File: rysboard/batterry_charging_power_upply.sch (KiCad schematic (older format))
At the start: 8 parts

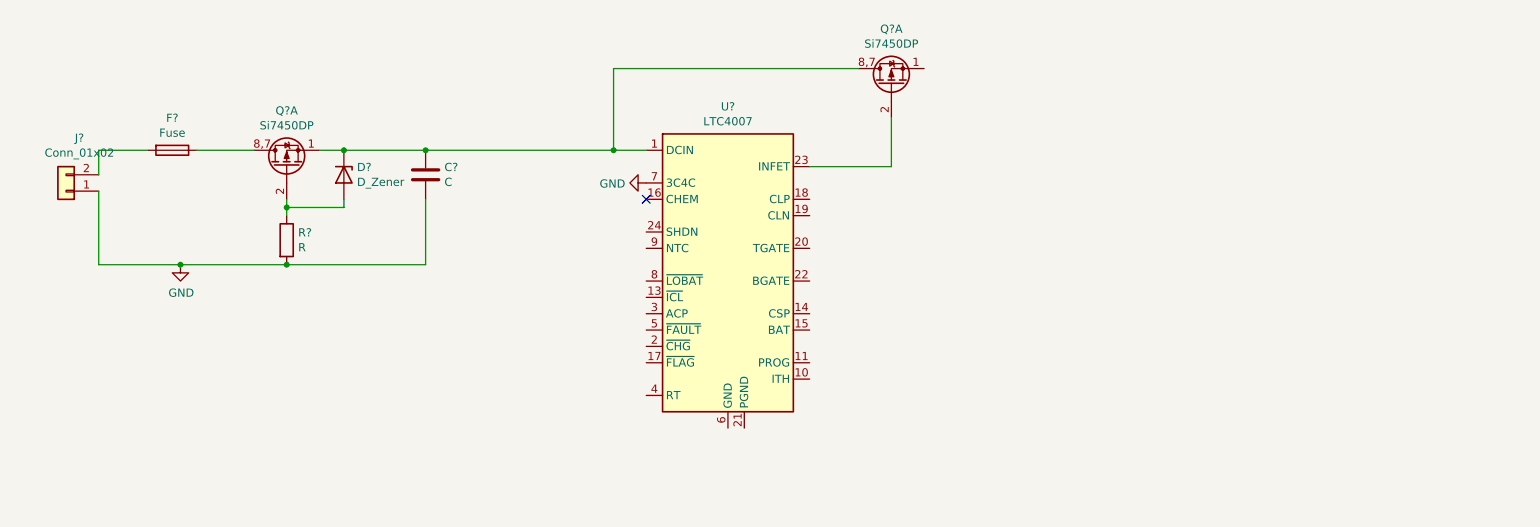
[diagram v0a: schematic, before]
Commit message: Added mcu, labeled its pins , major powwer supply overhaul started
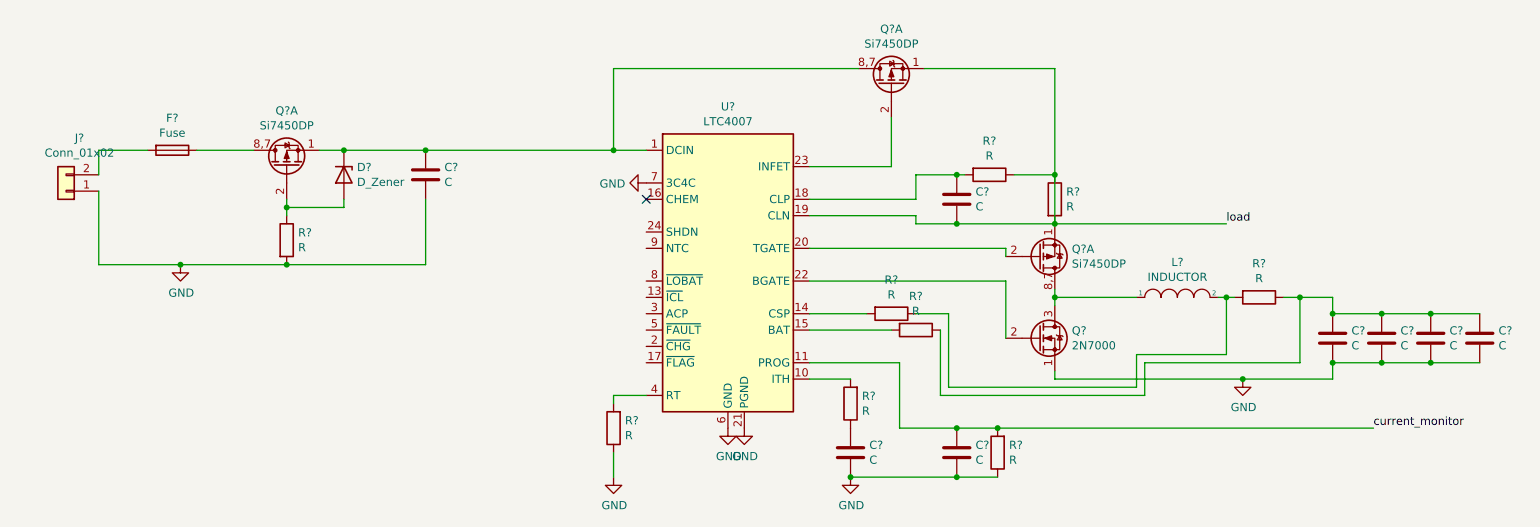
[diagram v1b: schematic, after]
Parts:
- added C? (x7): C, symbol Device:C
- added L?: INDUCTOR, symbol pspice:INDUCTOR
- added Q?: Si7450DP, Package_TO_SOT_SMD:SOT-23, symbol Transistor_FET:AO3401A
- added Q?: 2N7000, Package_TO_SOT_THT:TO-92_Inline, symbol Transistor_FET:2N7000
- added R? (x8): R, symbol Device:R
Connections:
- net GND: now also U?.21 (PGND), U?.6 (GND), C?.2, C?.2, C?.2, C?.2, C?.2, C?.2, Q?.1 (S), R?.1, R?.1
- net at U?.10 (ITH): now also R?.2
- net current_monitor: now reaches U?.11 (PROG)
- net current_monitor: now also C?.1, R?.2
- net at U?.14 (CSP): now also R?.2
- net at U?.15 (BAT): now also R?.2
- net at U?.18 (CLP): now also C?.1, R?.2
- net load: now reaches U?.19 (CLN)
- net load: now also Q?.1 (S1), C?.2, Q?.1 (S1), R?.1, R?.1, R?.2
- net at U?.20 (TGATE): now also Q?.2 (G1)
- net at U?.22 (BGATE): now also Q?.2 (G)
- net at U?.4 (RT): now also R?.2
- new net: L?.1, Q?.3 (D), Q?.8,7 (D1)
- new net: L?.2, R?.1, R?.2
- new net: C?.1, C?.1, C?.1, C?.1, R?.1, R?.1
- new net: C?.1, R?.1

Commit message: NST847BDP6T5G Added, more conections done
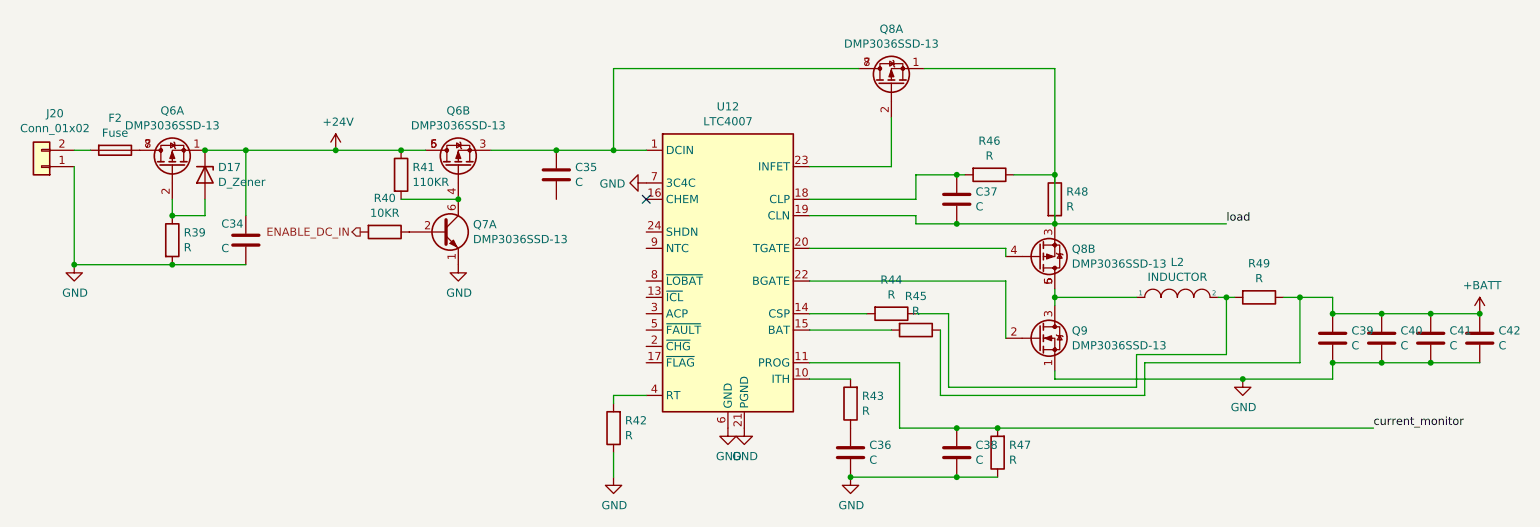
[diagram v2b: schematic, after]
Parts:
- removed Q? (x3): Si7450DP, Package_TO_SOT_SMD:SOT-23, symbol Transistor_FET:AO3401A
- added C34: C, symbol Device:C
- added Q6, Q8: DMP3036SSD-13, Package_SO:SO-8_5.3x6.2mm_P1.27mm, symbol rysboard:DMP3036SSD-13
- added Q7: DMP3036SSD-13, Package_SO:SO-8_5.3x6.2mm_P1.27mm, symbol rysboard:NST847BDP6T5G
- added R40: 10KR, symbol Device:R
- added R41: 110KR, symbol Device:R
- Q9: renamed from Q?; value 2N7000 -> DMP3036SSD-13; footprint Package_TO_SOT_THT:TO-92_Inline -> Package_SO:SO-8_5.3x6.2mm_P1.27mm
- gave numbers to parts that had none: 22
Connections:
- net GND: now also C34.2, Q7.1 (E1); no longer C35.2
- net load: now also Q8.1 (S1), Q8.3 (S2)
- net at C35.1, U12.1 (DCIN): now also Q6.3 (S2), Q8.7 (d), Q8.8 (d); no longer D17.1 (K)
- net at U12.20 (TGATE): now also Q8.4 (G2)
- net at U12.23 (INFET): now also Q8.2 (G1)
- net at D17.2 (A), R39.1: now also Q6.2 (G1)
- net at F2.1: now also Q6.7 (d), Q6.8 (d)
- net at L2.1, Q9.3 (D): now also Q8.5 (d), Q8.6 (d)
- net +BATT: now reaches C39.1, C40.1, C41.1, C42.1, R45.1, R49.1
- new net: Q6.4 (G2), Q7.6 (C1), R41.2
- new net: Q7.2 (B1), R40.1
- new net +24V: C34.1, D17.1 (K), Q6.1 (S1), Q6.5 (d), Q6.6 (d), R41.1
- new net ENABLE_DC_IN: R40.2
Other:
- moved on the sheet: C35, D17, F2, J20, R39

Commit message: created eval board for STM , added mcu, created controll section for TOFS and FAN. Added programming pinout, Remooved legacy spi interface, Removed addidtional i2c socket
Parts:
- removed Q7: DMP3036SSD-13, Package_SO:SO-8_5.3x6.2mm_P1.27mm, symbol rysboard:NST847BDP6T5G
- added Q?: NST847BDP6T5G, Package_TO_SOT_SMD:SOT-963, symbol rysboard:NST847BDP6T5G
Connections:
- net GND: now also C35.2, Q?.1 (E1)
- net at Q6.4 (G2), R41.2: now also Q?.6 (C1)
- net at R40.1: now also Q?.2 (B1)
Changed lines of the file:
@@
 $Descr A4 11693 8268
 encoding utf-8
-Sheet 4 6
+Sheet 4 7
 Title ""
 Date ""
@@
 	1650 1750 1550 1750
 $Comp
-L rysboard:NST847BDP6T5G Q7
-U 1 1 606ABC18
-P 3800 2250
-F 0 "Q7" H 3990 2296 50  0000 L CNN
-F 1 "DMP3036SSD-13" H 3990 2205 50  0000 L CNN
-F 2 "Package_SO:SO-8_5.3x6.2mm_P1.27mm" H 4000 2350 50  0001 C CNN
-F 3 "http://www.vishay.com/docs/70209/70209.pdf" H 3800 2250 50  0001 C CNN
-	1    3800 2250
-	1    0    0    -1
-$EndComp
-Connection ~ 3900 2050
-$Comp
 L power:GND #PWR041
 U 1 1 606AC403
@@
 	1    0    0    1
 $EndComp
+$Comp
+L rysboard:NST847BDP6T5G Q?
+U 1 1 606EA8D4
+P 3800 2250
+F 0 "Q?" H 3990 2296 50  0000 L CNN
+F 1 "NST847BDP6T5G" H 3990 2205 50  0000 L CNN
+F 2 "Package_TO_SOT_SMD:SOT-963" H 4000 2350 50  0001 C CNN
+F 3 "~" H 3800 2250 50  0001 C CNN
+	1    3800 2250
+	1    0    0    -1
+$EndComp
+Connection ~ 3900 2050
+$Comp
+L power:GND #PWR?
+U 1 1 606EB25B
+P 4500 2050
+F 0 "#PWR?" H 4500 1800 50  0001 C CNN
+F 1 "GND" H 4505 1877 50  0000 C CNN
+F 2 "" H 4500 2050 50  0001 C CNN
+F 3 "" H 4500 2050 50  0001 C CNN
+	1    4500 2050
+	1    0    0    -1
+$EndComp
 $EndSCHEMATC

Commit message: added some of the analog sensors
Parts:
- gave numbers to parts that had none: 1
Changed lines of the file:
@@
 $EndComp
 $Comp
-L rysboard:NST847BDP6T5G Q?
+L rysboard:NST847BDP6T5G Q7
 U 1 1 606EA8D4
 P 3800 2250
-F 0 "Q?" H 3990 2296 50  0000 L CNN
+F 0 "Q7" H 3990 2296 50  0000 L CNN
 F 1 "NST847BDP6T5G" H 3990 2205 50  0000 L CNN
 F 2 "Package_TO_SOT_SMD:SOT-963" H 4000 2350 50  0001 C CNN
@@
 Connection ~ 3900 2050
 $Comp
-L power:GND #PWR?
+L power:GND #PWR0101
 U 1 1 606EB25B
 P 4500 2050
-F 0 "#PWR?" H 4500 1800 50  0001 C CNN
+F 0 "#PWR0101" H 4500 1800 50  0001 C CNN
 F 1 "GND" H 4505 1877 50  0000 C CNN
 F 2 "" H 4500 2050 50  0001 C CNN

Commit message: sensors enable added, Vref problem to solve
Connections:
- net load renamed +12V
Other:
- note added: "REMOVE ADDITIONA L mosfet USE INTERNAL SHUDTOWN PIN"
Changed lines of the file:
@@
 	7550 1250 6750 1250
 Wire Wire Line
-	7550 2200 8600 2200
+	7550 2200 8500 2200
 $Comp
 L Transistor_FET:2N7000 Q9
@@
 current_monitor
 Text Label 8600 2200 0    50   ~ 0
-load
+EL_LOAD
 $Comp
 L Device:R R42
@@
 	1    0    0    -1
 $EndComp
+Text Notes 3050 1000 0    50   ~ 0
+REMOVE ADDITIONA L mosfet USE INTERNAL SHUDTOWN PIN
+$Comp
+L power:+12V #PWR?
+U 1 1 604387DC
+P 8500 2200
+F 0 "#PWR?" H 8500 2050 50  0001 C CNN
+F 1 "+12V" H 8515 2373 50  0000 C CNN
+F 2 "" H 8500 2200 50  0001 C CNN
+F 3 "" H 8500 2200 50  0001 C CNN
+	1    8500 2200
+	1    0    0    -1
+$EndComp
+Connection ~ 8500 2200
+Wire Wire Line
+	8500 2200 8600 2200
 $EndSCHEMATC

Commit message: new mosfet footprints
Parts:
- R40, R41: footprint (none) -> Resistor_SMD:R_0603_1608Metric
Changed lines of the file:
@@
 F 0 "R41" H 3620 1946 50  0000 L CNN
 F 1 "110KR" H 3620 1855 50  0000 L CNN
-F 2 "" V 3480 1900 50  0001 C CNN
+F 2 "Resistor_SMD:R_0603_1608Metric" V 3480 1900 50  0001 C CNN
 F 3 "~" H 3550 1900 50  0001 C CNN
 	1    3550 1900
@@
 F 0 "R40" V 3243 2250 50  0000 C CNN
 F 1 "10KR" V 3334 2250 50  0000 C CNN
-F 2 "" V 3380 2250 50  0001 C CNN
+F 2 "Resistor_SMD:R_0603_1608Metric" V 3380 2250 50  0001 C CNN
 F 3 "~" H 3450 2250 50  0001 C CNN
 	1    3450 2250
@@
 REMOVE ADDITIONA L mosfet USE INTERNAL SHUDTOWN PIN
 $Comp
-L power:+12V #PWR?
+L power:+12V #PWR061
 U 1 1 604387DC
 P 8500 2200
-F 0 "#PWR?" H 8500 2050 50  0001 C CNN
+F 0 "#PWR061" H 8500 2050 50  0001 C CNN
 F 1 "+12V" H 8515 2373 50  0000 C CNN
 F 2 "" H 8500 2200 50  0001 C CNN

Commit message: Fixed library, added a few MOSFET layouts
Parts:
- removed Q8: DMP3036SSD-13, Package_SO:SO-8_5.3x6.2mm_P1.27mm, symbol rysboard:DMP3036SSD-13
- removed Q9: DMP3036SSD-13, Package_SO:SO-8_5.3x6.2mm_P1.27mm, symbol Transistor_FET:2N7000
- removed R41: 110KR, Resistor_SMD:R_0603_1608Metric, symbol Device:R
- added Q5: DMP3036SSD-13, Package_SO:SO-8_3.9x4.9mm_P1.27mm, symbol rysboard:DMP3036SSD-13
- added Q?: Si7938DP-T1-GE3, Package_SO:PowerPAK_SO-8_Dual, symbol rysboard:Si7938DP-T1-GE3
- Q6: footprint Package_SO:SO-8_5.3x6.2mm_P1.27mm -> Package_SO:SO-8_3.9x4.9mm_P1.27mm
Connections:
- net +12V: now also Q6.3 (S2), Q6.7 (d), Q6.8 (d)
- net +24V: now also C35.1, U12.1 (DCIN), Q5.3 (S2); no longer Q6.5 (d), Q6.6 (d)
- net GND: now also Q?.3 (S2)
- net at U12.20 (TGATE): now also Q6.4 (G2)
- net at U12.22 (BGATE): now also Q?.4 (G2)
- net at U12.23 (INFET): now also Q6.2 (G1)
- net at D17.2 (A), R39.1: now also Q5.4 (G2); no longer Q6.2 (G1)
- net at L2.1: now also Q6.5 (d), Q6.6 (d), Q?.6 (D1)
- net at Q7.6 (C1): no longer Q6.4 (G2)
- new net: F2.1, Q5.5 (d), Q5.6 (d)
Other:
- moved on the sheet: Q7A, R40
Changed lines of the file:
@@
 Wire Wire Line
 	7550 2200 8500 2200
-$Comp
-L Transistor_FET:2N7000 Q9
-U 1 1 5FF132A9
-P 7450 2900
-F 0 "Q9" H 7654 2946 50  0000 L CNN
-F 1 "DMP3036SSD-13" H 7654 2855 50  0000 L CNN
-F 2 "Package_SO:SO-8_5.3x6.2mm_P1.27mm" H 7650 2825 50  0001 L CIN
-F 3 "http://www.vishay.com/docs/70209/70209.pdf" H 7450 2900 50  0001 L CNN
-	1    7450 2900
-	1    0    0    -1
-$EndComp
 Wire Wire Line
 	7550 2700 7550 2650
@@
 Wire Wire Line
 	1550 1850 1550 2450
-$Comp
-L rysboard:DMP3036SSD-13 Q6
-U 1 1 606882F4
-P 2150 1850
-F 0 "Q6" V 2492 1850 50  0000 C CNN
-F 1 "DMP3036SSD-13" V 2401 1850 50  0000 C CNN
-F 2 "Package_SO:SO-8_5.3x6.2mm_P1.27mm" H 2350 1775 50  0001 L CIN
-F 3 "http://www.vishay.com/docs/70209/70209.pdf" H 2150 1850 50  0001 L CNN
-	1    2150 1850
-	0    -1   -1   0
-$EndComp
-$Comp
-L rysboard:DMP3036SSD-13 Q6
-U 2 1 60689C49
-P 3900 1850
-F 0 "Q6" V 4242 1850 50  0000 C CNN
-F 1 "DMP3036SSD-13" V 4151 1850 50  0000 C CNN
-F 2 "Package_SO:SO-8_5.3x6.2mm_P1.27mm" H 4100 1775 50  0001 L CIN
-F 3 "http://www.vishay.com/docs/70209/70209.pdf" H 3900 1850 50  0001 L CNN
-	2    3900 1850
-	0    -1   -1   0
-$EndComp
 Connection ~ 1550 2450
 Connection ~ 4500 1750
@@
 	1    0    0    -1
 $EndComp
-Wire Wire Line
-	3700 1750 3550 1750
-Wire Wire Line
-	4100 1750 4500 1750
-$Comp
-L Device:R R41
-U 1 1 606A1005
-P 3550 1900
-F 0 "R41" H 3620 1946 50  0000 L CNN
-F 1 "110KR" H 3620 1855 50  0000 L CNN
-F 2 "Resistor_SMD:R_0603_1608Metric" V 3480 1900 50  0001 C CNN
-F 3 "~" H 3550 1900 50  0001 C CNN
-	1    3550 1900
-	1    0    0    -1
-$EndComp
-Connection ~ 3550 1750
 Connection ~ 3150 1750
 Wire Wire Line
-	3150 1750 3550 1750
-Wire Wire Line
-	3550 2050 3900 2050
-Wire Wire Line
 	1650 1750 1550 1750
-$Comp
-L power:GND #PWR041
-U 1 1 606AC403
-P 3900 2450
-F 0 "#PWR041" H 3900 2200 50  0001 C CNN
-F 1 "GND" H 3905 2277 50  0000 C CNN
-F 2 "" H 3900 2450 50  0001 C CNN
-F 3 "" H 3900 2450 50  0001 C CNN
-	1    3900 2450
-	1    0    0    -1
-$EndComp
-$Comp
-L Device:R R40
-U 1 1 606AC756
-P 3450 2250
-F 0 "R40" V 3243 2250 50  0000 C CNN
-F 1 "10KR" V 3334 2250 50  0000 C CNN
-F 2 "Resistor_SMD:R_0603_1608Metric" V 3380 2250 50  0001 C CNN
-F 3 "~" H 3450 2250 50  0001 C CNN
-	1    3450 2250
-	0    1    1    0
-$EndComp
-Text HLabel 3300 2250 0    50   Output ~ 0
-ENABLE_DC_IN
 Connection ~ 2150 2450
 Wire Wire Line
@@
 Wire Wire Line
 	2350 1750 2600 1750
-Connection ~ 2350 1750
 Wire Wire Line
 	2350 2150 2150 2150
@@
 Wire Wire Line
 	2600 2150 2600 1750
-$Comp
-L rysboard:DMP3036SSD-13 Q8
-U 1 1 606CBDEE
-P 6550 1350
-F 0 "Q8" V 6892 1350 50  0000 C CNN
-F 1 "DMP3036SSD-13" V 6801 1350 50  0000 C CNN
-F 2 "Package_SO:SO-8_5.3x6.2mm_P1.27mm" H 6750 1275 50  0001 L CIN
-F 3 "http://www.vishay.com/docs/70209/70209.pdf" H 6550 1350 50  0001 L CNN
-	1    6550 1350
-	0    -1   -1   0
-$EndComp
-$Comp
-L rysboard:DMP3036SSD-13 Q8
-U 2 1 606CD530
-P 7450 2400
-F 0 "Q8" H 7654 2354 50  0000 L CNN
-F 1 "DMP3036SSD-13" H 7654 2445 50  0000 L CNN
-F 2 "Package_SO:SO-8_5.3x6.2mm_P1.27mm" H 7650 2325 50  0001 L CIN
-F 3 "http://www.vishay.com/docs/70209/70209.pdf" H 7450 2400 50  0001 L CNN
-	2    7450 2400
-	1    0    0    1
-$EndComp
-$Comp
-L rysboard:NST847BDP6T5G Q7
-U 1 1 606EA8D4
-P 3800 2250
-F 0 "Q7" H 3990 2296 50  0000 L CNN
-F 1 "NST847BDP6T5G" H 3990 2205 50  0000 L CNN
-F 2 "Package_TO_SOT_SMD:SOT-963" H 4000 2350 50  0001 C CNN
-F 3 "~" H 3800 2250 50  0001 C CNN
-	1    3800 2250
-	1    0    0    -1
-$EndComp
-Connection ~ 3900 2050
 $Comp
 L power:GND #PWR0101
@@
 Wire Wire Line
 	8500 2200 8600 2200
+$Comp
+L power:GND #PWR041
+U 1 1 606AC403
+P 3900 3000
+F 0 "#PWR041" H 3900 2750 50  0001 C CNN
+F 1 "GND" H 3905 2827 50  0000 C CNN
+F 2 "" H 3900 3000 50  0001 C CNN
+F 3 "" H 3900 3000 50  0001 C CNN
+	1    3900 3000
+	1    0    0    -1
+$EndComp
+$Comp
+L Device:R R40
+U 1 1 606AC756
+P 3450 2800
+F 0 "R40" V 3243 2800 50  0000 C CNN
+F 1 "10KR" V 3334 2800 50  0000 C CNN
+F 2 "Resistor_SMD:R_0603_1608Metric" V 3380 2800 50  0001 C CNN
+F 3 "~" H 3450 2800 50  0001 C CNN
+	1    3450 2800
+	0    1    1    0
+$EndComp
+Text HLabel 3300 2800 0    50   Output ~ 0
+ENABLE_DC_IN
+$Comp
+L rysboard:NST847BDP6T5G Q7
+U 1 1 606EA8D4
+P 3800 2800
+F 0 "Q7" H 3990 2846 50  0000 L CNN
+F 1 "NST847BDP6T5G" H 3990 2755 50  0000 L CNN
+F 2 "Package_TO_SOT_SMD:SOT-963" H 4000 2900 50  0001 C CNN
+F 3 "~" H 3800 2800 50  0001 C CNN
+	1    3800 2800
+	1    0    0    -1
+$EndComp
+Wire Wire Line
+	3150 1750 4500 1750
+$Comp
+L rysboard:DMP3036SSD-13 Q5
+U 2 1 6050A980
+P 2150 1850
+F 0 "Q5" V 2492 1850 50  0000 C CNN
+F 1 "DMP3036SSD-13" V 2401 1850 50  0000 C CNN
+F 2 "Package_SO:SO-8_3.9x4.9mm_P1.27mm" H 2350 1775 50  0001 L CIN
+F 3 "" H 2150 1850 50  0001 L CNN
+	2    2150 1850
+	0    -1   -1   0
+$EndComp
+Connection ~ 2350 1750
+$Comp
+L rysboard:DMP3036SSD-13 Q6
+U 1 1 6050BA61
+P 6550 1350
+F 0 "Q6" V 6892 1350 50  0000 C CNN
+F 1 "DMP3036SSD-13" V 6801 1350 50  0000 C CNN
+F 2 "Package_SO:SO-8_3.9x4.9mm_P1.27mm" H 6750 1275 50  0001 L CIN
+F 3 "" H 6550 1350 50  0001 L CNN
+	1    6550 1350
+	0    1    -1   0
+$EndComp
+$Comp
+L rysboard:DMP3036SSD-13 Q6
+U 2 1 6051AD38
+P 7450 2400
+F 0 "Q6" H 7654 2354 50  0000 L CNN
+F 1 "DMP3036SSD-13" H 7654 2445 50  0000 L CNN
+F 2 "Package_SO:SO-8_3.9x4.9mm_P1.27mm" H 7650 2325 50  0001 L CIN
+F 3 "" H 7450 2400 50  0001 L CNN
+	2    7450 2400
+	1    0    0    1
+$EndComp
+$Comp
+L rysboard:Si7938DP-T1-GE3 Q?
+U 2 1 605E9857
+P 7450 2900
+F 0 "Q?" H 7654 2946 50  0000 L CNN
+F 1 "Si7938DP-T1-GE3" H 7654 2855 50  0000 L CNN
+F 2 "Package_SO:PowerPAK_SO-8_Dual" H 7650 2825 50  0001 L CIN
+F 3 "" H 7450 2900 50  0001 L CNN
+	2    7450 2900
+	1    0    0    -1
+$EndComp
 $EndSCHEMATC

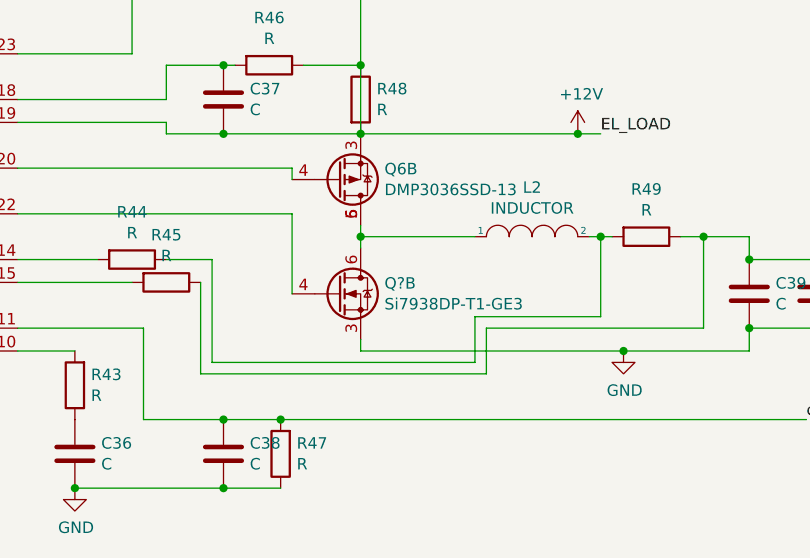
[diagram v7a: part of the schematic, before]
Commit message: battery Balancing specified
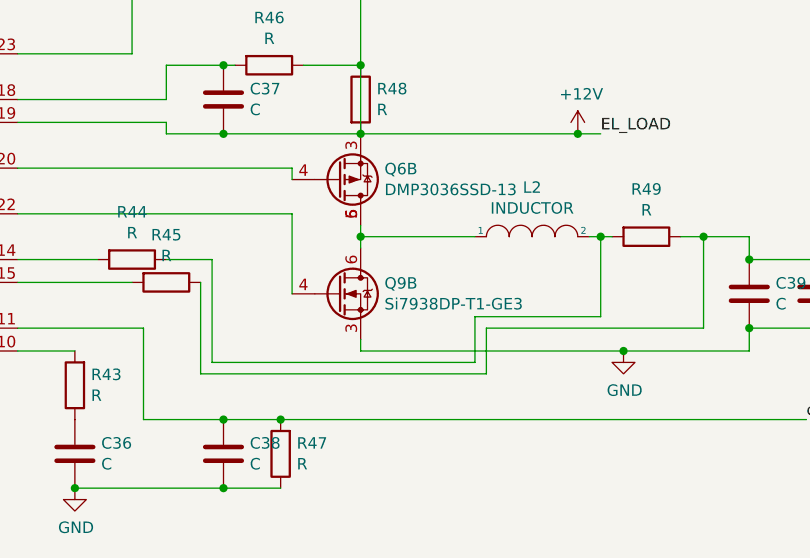
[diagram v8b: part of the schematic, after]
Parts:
- gave numbers to parts that had none: 1
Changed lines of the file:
@@
 $EndComp
 $Comp
-L rysboard:Si7938DP-T1-GE3 Q?
+L rysboard:Si7938DP-T1-GE3 Q9
 U 2 1 605E9857
 P 7450 2900
-F 0 "Q?" H 7654 2946 50  0000 L CNN
+F 0 "Q9" H 7654 2946 50  0000 L CNN
 F 1 "Si7938DP-T1-GE3" H 7654 2855 50  0000 L CNN
 F 2 "Package_SO:PowerPAK_SO-8_Dual" H 7650 2825 50  0001 L CIN
